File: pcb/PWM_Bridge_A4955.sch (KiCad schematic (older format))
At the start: 18 parts, among them Q3 IPD220N06L3, Q4 IPD220N06L3, Q5 IPD220N06L3, Q6 IPD220N06L3, U5 A4955GLPTR-T

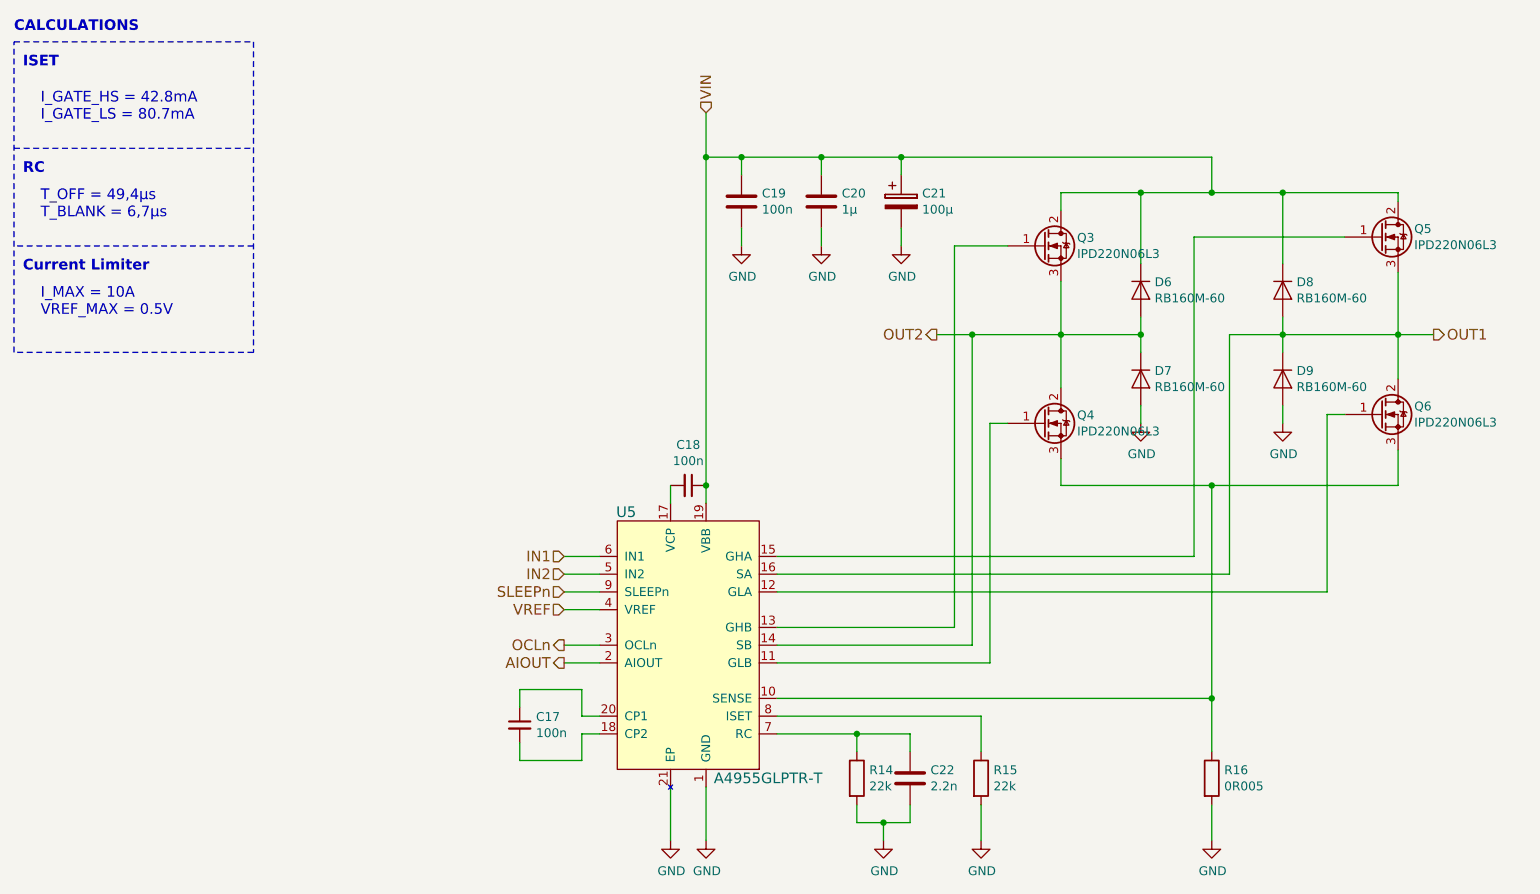
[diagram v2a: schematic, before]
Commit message: Improve layout and add voltage sensing circuit to layout
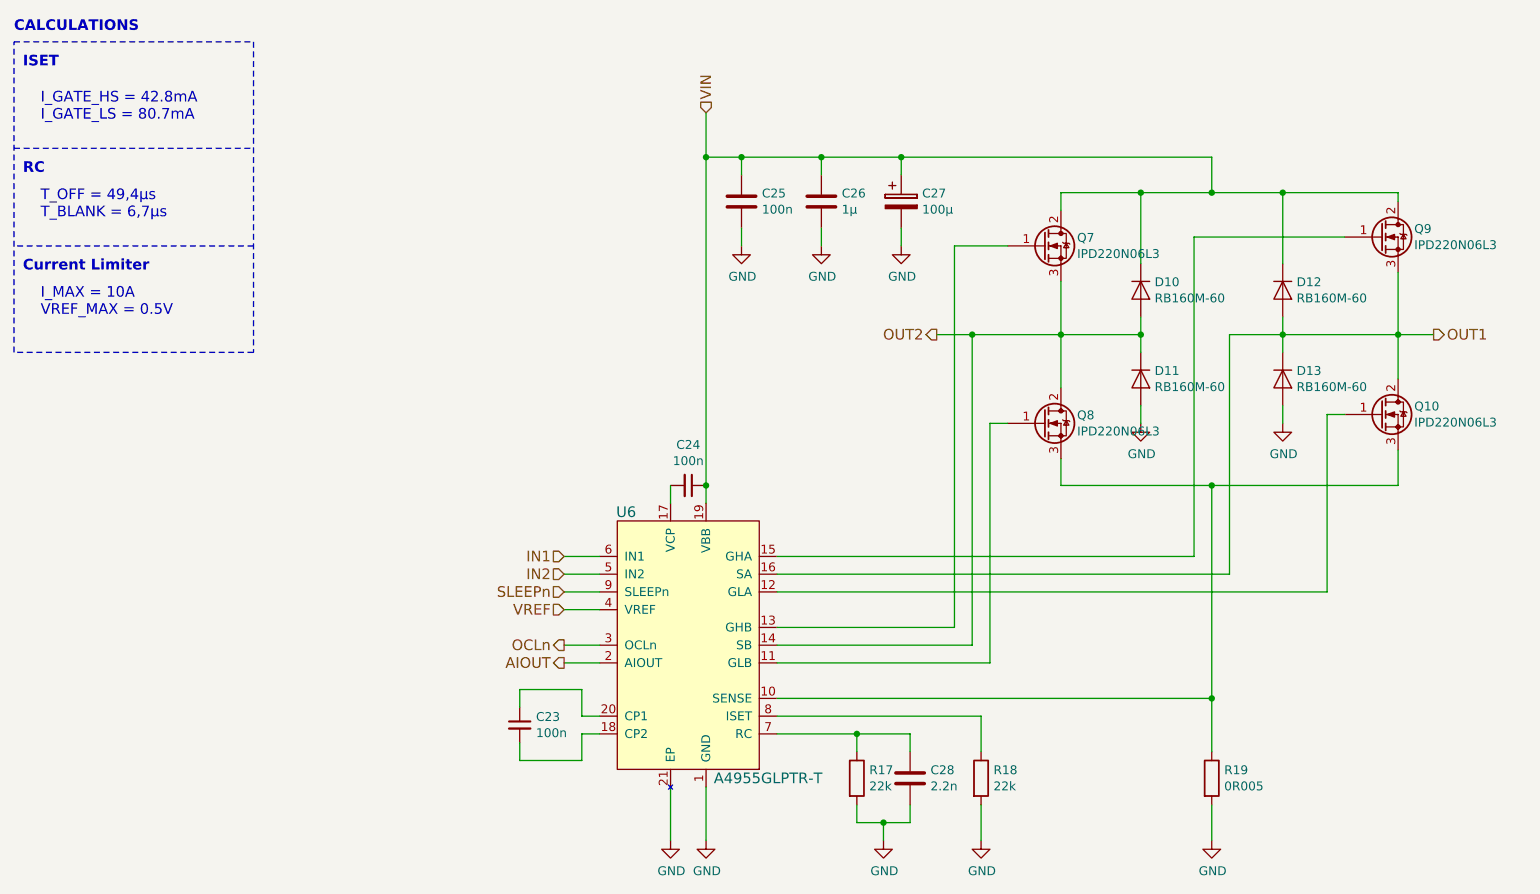
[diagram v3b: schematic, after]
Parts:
- Q3, Q4, Q5, Q6: footprint TO_SOT_Packages_SMD:TO-252-2Lead -> TO_SOT_Packages_SMD_local:PG-TO-252-3-313

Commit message: Add some improvements, fix issue with schematic error
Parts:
- Q3, Q4, Q5, Q6: value IPD220N06L3 -> IPD079N06L3G; Digi-Key Minimum Quantity (none) -> 1; Digi-Key Part Number (none) -> IPD079N06L3 GCT-ND
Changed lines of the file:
@@
 LIBS:a4955glptr-t
 LIBS:ap2112k-3.3trg1
+LIBS:lm75bd
+LIBS:mechanical
 LIBS:HighPower-Mechaduino-cache
 EELAYER 25 0
@@
 $EndComp
 $Comp
-L GND #PWR066
+L GND #PWR070
 U 1 1 580787DB
 P 5750 5500
-AR Path="/58077727/580787DB" Ref="#PWR066"  Part="1"
-AR Path="/58084D17/580787DB" Ref="#PWR076"  Part="1"
-F 0 "#PWR076" H 5750 5250 50  0001 C CNN
+AR Path="/58077727/580787DB" Ref="#PWR070"  Part="1"
+AR Path="/58084D17/580787DB" Ref="#PWR080"  Part="1"
+F 0 "#PWR080" H 5750 5250 50  0001 C CNN
 F 1 "GND" H 5755 5327 50  0000 C CNN
 F 2 "" H 5750 5500 50  0000 C CNN
@@
 $EndComp
 $Comp
-L GND #PWR067
+L GND #PWR071
 U 1 1 58078835
 P 4750 5500
-AR Path="/58077727/58078835" Ref="#PWR067"  Part="1"
-AR Path="/58084D17/58078835" Ref="#PWR077"  Part="1"
-F 0 "#PWR077" H 4750 5250 50  0001 C CNN
+AR Path="/58077727/58078835" Ref="#PWR071"  Part="1"
+AR Path="/58084D17/58078835" Ref="#PWR081"  Part="1"
+F 0 "#PWR081" H 4750 5250 50  0001 C CNN
 F 1 "GND" H 4755 5327 50  0000 C CNN
 F 2 "" H 4750 5500 50  0000 C CNN
@@
 $EndComp
 $Comp
-L GND #PWR068
+L GND #PWR072
 U 1 1 58078AB1
 P 7600 5500
-AR Path="/58077727/58078AB1" Ref="#PWR068"  Part="1"
-AR Path="/58084D17/58078AB1" Ref="#PWR078"  Part="1"
-F 0 "#PWR078" H 7600 5250 50  0001 C CNN
+AR Path="/58077727/58078AB1" Ref="#PWR072"  Part="1"
+AR Path="/58084D17/58078AB1" Ref="#PWR082"  Part="1"
+F 0 "#PWR082" H 7600 5250 50  0001 C CNN
 F 1 "GND" H 7605 5327 50  0000 C CNN
 F 2 "" H 7600 5500 50  0000 C CNN
@@
 AR Path="/58084D17/58078C46" Ref="Q7"  Part="1"
 F 0 "Q7" H 6841 2196 50  0000 L CNN
-F 1 "IPD220N06L3" H 6841 2105 50  0000 L CNN
+F 1 "IPD079N06L3G" H 6841 2105 50  0000 L CNN
 F 2 "TO_SOT_Packages_SMD_local:PG-TO-252-3-313" H 6850 2250 50  0001 C CNN
-F 3 "" H 6650 2150 50  0000 C CNN
+F 3 "http://www.infineon.com/dgdl/IPD079N06L3_Rev2.0.pdf?folderId=db3a30431441fb5d01148ca9f1be0e77&fileId=db3a30431ddc9372011e2b5528634dc0" H 6650 2150 50  0001 C CNN
+F 4 "IPD079N06L3 GCT-ND" H 6650 2150 60  0001 C CNN "Digi-Key Part Number"
+F 5 "1" H 6650 2150 60  0001 C CNN "Digi-Key Minimum Quantity"
 	1    6650 2150
 	1    0    0    -1
@@
 AR Path="/58084D17/58078E80" Ref="Q9"  Part="1"
 F 0 "Q9" H 8741 2146 50  0000 L CNN
-F 1 "IPD220N06L3" H 8741 2055 50  0000 L CNN
+F 1 "IPD079N06L3G" H 8741 2055 50  0000 L CNN
 F 2 "TO_SOT_Packages_SMD_local:PG-TO-252-3-313" H 8750 2200 50  0001 C CNN
-F 3 "" H 8550 2100 50  0000 C CNN
+F 3 "http://www.infineon.com/dgdl/IPD079N06L3_Rev2.0.pdf?folderId=db3a30431441fb5d01148ca9f1be0e77&fileId=db3a30431ddc9372011e2b5528634dc0" H 8550 2100 50  0001 C CNN
+F 4 "IPD079N06L3 GCT-ND" H 8550 2100 60  0001 C CNN "Digi-Key Part Number"
+F 5 "1" H 8550 2100 60  0001 C CNN "Digi-Key Minimum Quantity"
 	1    8550 2100
 	1    0    0    -1
@@
 AR Path="/58084D17/58078ED9" Ref="Q10"  Part="1"
 F 0 "Q10" H 8741 3146 50  0000 L CNN
-F 1 "IPD220N06L3" H 8741 3055 50  0000 L CNN
+F 1 "IPD079N06L3G" H 8741 3055 50  0000 L CNN
 F 2 "TO_SOT_Packages_SMD_local:PG-TO-252-3-313" H 8750 3200 50  0001 C CNN
-F 3 "" H 8550 3100 50  0000 C CNN
+F 3 "http://www.infineon.com/dgdl/IPD079N06L3_Rev2.0.pdf?folderId=db3a30431441fb5d01148ca9f1be0e77&fileId=db3a30431ddc9372011e2b5528634dc0" H 8550 3100 50  0001 C CNN
+F 4 "IPD079N06L3 GCT-ND" H 8550 3100 60  0001 C CNN "Digi-Key Part Number"
+F 5 "1" H 8550 3100 60  0001 C CNN "Digi-Key Minimum Quantity"
 	1    8550 3100
 	1    0    0    -1
@@
 AR Path="/58084D17/58078F3F" Ref="Q8"  Part="1"
 F 0 "Q8" H 6841 3196 50  0000 L CNN
-F 1 "IPD220N06L3" H 6841 3105 50  0000 L CNN
+F 1 "IPD079N06L3G" H 6841 3105 50  0000 L CNN
 F 2 "TO_SOT_Packages_SMD_local:PG-TO-252-3-313" H 6850 3250 50  0001 C CNN
-F 3 "" H 6650 3150 50  0000 C CNN
+F 3 "http://www.infineon.com/dgdl/IPD079N06L3_Rev2.0.pdf?folderId=db3a30431441fb5d01148ca9f1be0e77&fileId=db3a30431ddc9372011e2b5528634dc0" H 6650 3150 50  0001 C CNN
+F 4 "IPD079N06L3 GCT-ND" H 6650 3150 60  0001 C CNN "Digi-Key Part Number"
+F 5 "1" H 6650 3150 60  0001 C CNN "Digi-Key Minimum Quantity"
 	1    6650 3150
 	1    0    0    -1
@@
 $EndComp
 $Comp
-L GND #PWR069
+L GND #PWR073
 U 1 1 5807A4C6
 P 4950 2150
-AR Path="/58077727/5807A4C6" Ref="#PWR069"  Part="1"
-AR Path="/58084D17/5807A4C6" Ref="#PWR079"  Part="1"
-F 0 "#PWR079" H 4950 1900 50  0001 C CNN
+AR Path="/58077727/5807A4C6" Ref="#PWR073"  Part="1"
+AR Path="/58084D17/5807A4C6" Ref="#PWR083"  Part="1"
+F 0 "#PWR083" H 4950 1900 50  0001 C CNN
 F 1 "GND" H 4955 1977 50  0000 C CNN
 F 2 "" H 4950 2150 50  0000 C CNN
@@
 $EndComp
 $Comp
-L GND #PWR070
+L GND #PWR074
 U 1 1 5807A964
 P 5850 2150
-AR Path="/58077727/5807A964" Ref="#PWR070"  Part="1"
-AR Path="/58084D17/5807A964" Ref="#PWR080"  Part="1"
-F 0 "#PWR080" H 5850 1900 50  0001 C CNN
+AR Path="/58077727/5807A964" Ref="#PWR074"  Part="1"
+AR Path="/58084D17/5807A964" Ref="#PWR084"  Part="1"
+F 0 "#PWR084" H 5850 1900 50  0001 C CNN
 F 1 "GND" H 5855 1977 50  0000 C CNN
 F 2 "" H 5850 2150 50  0000 C CNN
@@
 $EndComp
 $Comp
-L GND #PWR081
+L GND #PWR085
 U 1 1 5809ACB6
 P 5400 2150
-AR Path="/58084D17/5809ACB6" Ref="#PWR081"  Part="1"
-AR Path="/58077727/5809ACB6" Ref="#PWR071"  Part="1"
-F 0 "#PWR081" H 5400 1900 50  0001 C CNN
+AR Path="/58084D17/5809ACB6" Ref="#PWR085"  Part="1"
+AR Path="/58077727/5809ACB6" Ref="#PWR075"  Part="1"
+F 0 "#PWR085" H 5400 1900 50  0001 C CNN
 F 1 "GND" H 5405 1977 50  0000 C CNN
 F 2 "" H 5400 2150 50  0000 C CNN
@@
 $EndComp
 $Comp
-L GND #PWR072
+L GND #PWR076
 U 1 1 580A46B3
 P 6300 5500
-AR Path="/58077727/580A46B3" Ref="#PWR072"  Part="1"
-AR Path="/58084D17/580A46B3" Ref="#PWR082"  Part="1"
-F 0 "#PWR082" H 6300 5250 50  0001 C CNN
+AR Path="/58077727/580A46B3" Ref="#PWR076"  Part="1"
+AR Path="/58084D17/580A46B3" Ref="#PWR086"  Part="1"
+F 0 "#PWR086" H 6300 5250 50  0001 C CNN
 F 1 "GND" H 6305 5327 50  0000 C CNN
 F 2 "" H 6300 5500 50  0000 C CNN
@@
 $EndComp
 $Comp
-L GND #PWR073
+L GND #PWR077
 U 1 1 581550B7
 P 8000 3150
-AR Path="/58077727/581550B7" Ref="#PWR073"  Part="1"
-AR Path="/58084D17/581550B7" Ref="#PWR083"  Part="1"
-F 0 "#PWR083" H 8000 2900 50  0001 C CNN
+AR Path="/58077727/581550B7" Ref="#PWR077"  Part="1"
+AR Path="/58084D17/581550B7" Ref="#PWR087"  Part="1"
+F 0 "#PWR087" H 8000 2900 50  0001 C CNN
 F 1 "GND" H 8005 2977 50  0000 C CNN
 F 2 "" H 8000 3150 50  0000 C CNN
@@
 $EndComp
 $Comp
-L GND #PWR074
+L GND #PWR078
 U 1 1 58155164
 P 7200 3150
-AR Path="/58077727/58155164" Ref="#PWR074"  Part="1"
-AR Path="/58084D17/58155164" Ref="#PWR084"  Part="1"
-F 0 "#PWR084" H 7200 2900 50  0001 C CNN
+AR Path="/58077727/58155164" Ref="#PWR078"  Part="1"
+AR Path="/58084D17/58155164" Ref="#PWR088"  Part="1"
+F 0 "#PWR088" H 7200 2900 50  0001 C CNN
 F 1 "GND" H 7205 2977 50  0000 C CNN
 F 2 "" H 7200 3150 50  0000 C CNN
@@
 	850  2750 850  1000
 $Comp
-L GND #PWR075
+L GND #PWR079
 U 1 1 582EE915
 P 4550 5500
-AR Path="/58077727/582EE915" Ref="#PWR075"  Part="1"
-AR Path="/58084D17/582EE915" Ref="#PWR085"  Part="1"
-F 0 "#PWR085" H 4550 5250 50  0001 C CNN
+AR Path="/58077727/582EE915" Ref="#PWR079"  Part="1"
+AR Path="/58084D17/582EE915" Ref="#PWR089"  Part="1"
+F 0 "#PWR089" H 4550 5250 50  0001 C CNN
 F 1 "GND" H 4555 5327 50  0000 C CNN
 F 2 "" H 4550 5500 50  0000 C CNN
